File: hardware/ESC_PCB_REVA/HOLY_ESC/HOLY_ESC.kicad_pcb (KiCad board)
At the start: 4 copper layers, 69.1 x 39.2 mm, 77 parts, among them J1 Header, J2 Conn_01x06_Pin, J3 Header, Q1 BUK7Y1R4-40H, Q2 BUK7Y1R4-40H, Q3 BUK7Y1R4-40H, Q4 BUK7Y1R4-40H, Q5 BUK7Y1R4-40H, Q6 BUK7Y1R4-40H, U1 DRV8300DPWR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

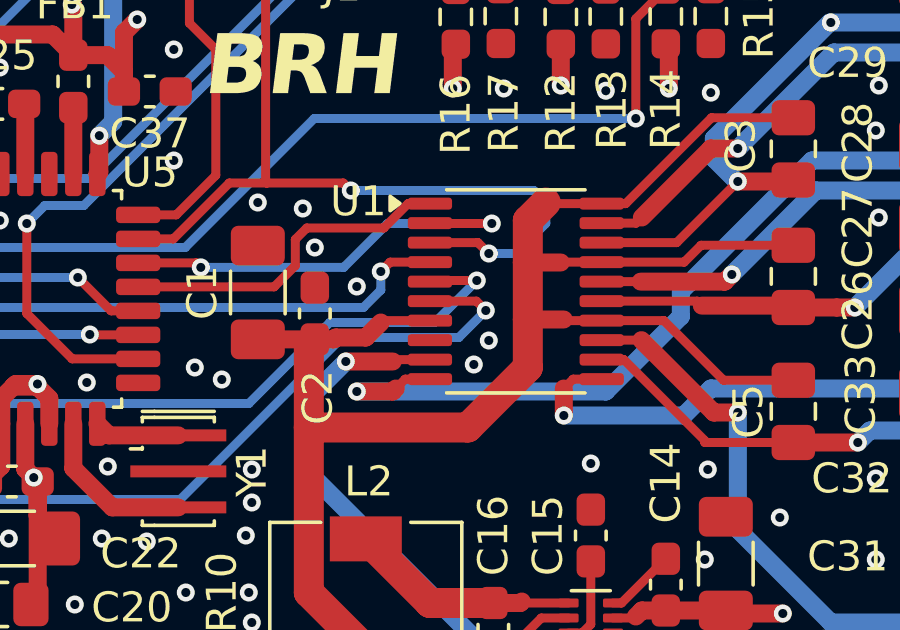
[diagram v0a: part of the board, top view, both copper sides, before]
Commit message: fix the REV A bst cap issue
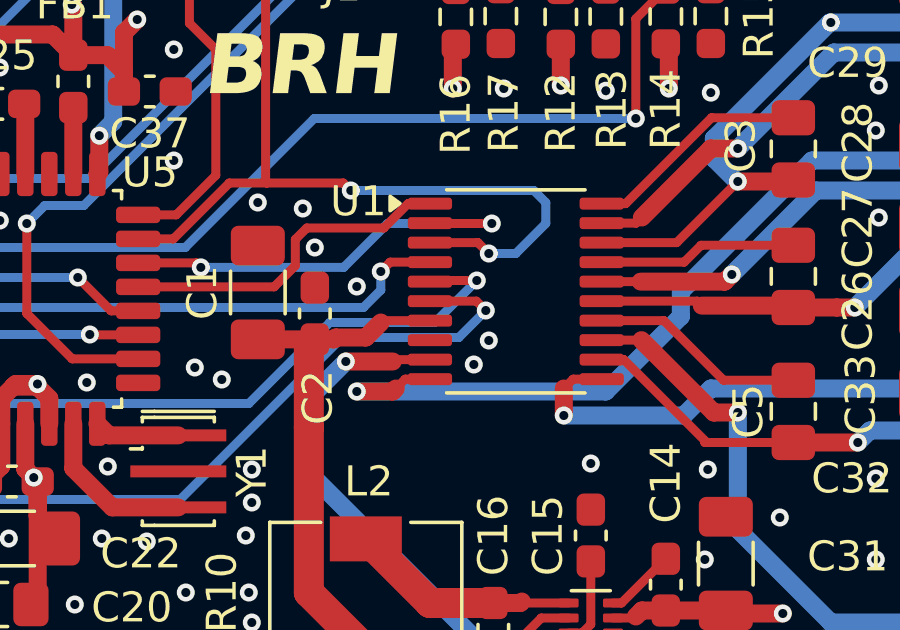
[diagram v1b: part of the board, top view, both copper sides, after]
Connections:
- C3 pad 1: +12V -> Net-(U1-BSTA)
- C4 pad 1: +12V -> Net-(U1-BSTB)
- C5 pad 1: +12V -> Net-(U1-BSTC)
- U1 pad 14: +12V -> Net-(U1-BSTC)
- U1 pad 17: +12V -> Net-(U1-BSTB)
- U1 pad 20: +12V -> Net-(U1-BSTA)
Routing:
- net +12V: track 90.7 -> 48.5 mm
- net Net-(U1-BSTA): track 0.00 -> 7.57 mm
- net Net-(U1-BSTC): track 0.00 -> 7.21 mm
- net Net-(U1-BSTB): track 0.00 -> 6.62 mm
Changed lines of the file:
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@@
 	(net 54 "Net-(D1-A)")
 	(net 55 "Net-(D2-A)")
+	(net 56 "Net-(U1-BSTA)")
+	(net 57 "Net-(U1-BSTB)")
+	(net 58 "Net-(U1-BSTC)")
 	(footprint "Package_TO_SOT_SMD:SOT-583-8"
 		(layer "F.Cu")
@@
 			(layers "F.Cu" "F.Mask" "F.Paste")
 			(roundrect_rratio 0.212766)
-			(net 1 "+12V")
+			(net 58 "Net-(U1-BSTC)")
 			(pintype "passive")
 		)
@@
 			(layers "F.Cu" "F.Mask" "F.Paste")
 			(roundrect_rratio 0.25)
-			(net 1 "+12V")
+			(net 58 "Net-(U1-BSTC)")
 			(pinfunction "BSTC")
 			(pintype "input")
@@
 			(layers "F.Cu" "F.Mask" "F.Paste")
 			(roundrect_rratio 0.25)
-			(net 1 "+12V")
+			(net 57 "Net-(U1-BSTB)")
 			(pinfunction "BSTB")
 			(pintype "input")
@@
 			(layers "F.Cu" "F.Mask" "F.Paste")
 			(roundrect_rratio 0.25)
-			(net 1 "+12V")
+			(net 56 "Net-(U1-BSTA)")
 			(pinfunction "BSTA")
 			(pintype "input")
@@
 			(layers "F.Cu" "F.Mask" "F.Paste")
 			(roundrect_rratio 0.212766)
-			(net 1 "+12V")
+			(net 56 "Net-(U1-BSTA)")
 			(pintype "passive")
 		)
@@
 			(layers "F.Cu" "F.Mask" "F.Paste")
 			(roundrect_rratio 0.212766)
-			(net 1 "+12V")
+			(net 57 "Net-(U1-BSTB)")
 			(pintype "passive")
 		)
@@
 	)
 	(segment
-		(start 173.675 82.325)
-		(end 176.75 82.325)
-		(width 0.3)
-		(layer "F.Cu")
-		(net 1)
-	)
-	(segment
 		(start 154.8625 99.9375)
 		(end 153.1875 101.6125)
@@
 	)
 	(segment
-		(start 167.9 86.4)
-		(end 167.9 84.8)
-		(width 1)
-		(layer "F.Cu")
-		(net 1)
-	)
-	(segment
-		(start 167.9 81.5)
-		(end 168.5 80.9)
-		(width 1)
-		(layer "F.Cu")
-		(net 1)
-	)
-	(segment
-		(start 169.0125 82.8875)
-		(end 169 82.9)
-		(width 0.3)
-		(layer "F.Cu")
-		(net 1)
-	)
-	(segment
-		(start 170.3625 80.9375)
-		(end 171.1625 80.9375)
-		(width 0.3)
-		(layer "F.Cu")
-		(net 1)
-	)
-	(segment
 		(start 153.1875 101.6125)
 		(end 150.825 101.6125)
@@
 	)
 	(segment
-		(start 167.9 84.8)
-		(end 167.9 82.9)
-		(width 1)
-		(layer "F.Cu")
-		(net 1)
-	)
-	(segment
 		(start 162.5 97.6125)
 		(end 162.5 99.2)
@@
 	)
 	(segment
-		(start 174.425 86.825)
-		(end 176.75 86.825)
-		(width 0.3)
-		(layer "F.Cu")
-		(net 1)
-	)
-	(segment
 		(start 164.2 99.25)
 		(end 162.55 99.25)
@@
 	)
 	(segment
-		(start 173.1125 82.8875)
-		(end 173.675 82.325)
-		(width 0.3)
-		(layer "F.Cu")
-		(net 1)
-	)
-	(segment
-		(start 167.9 82.9)
-		(end 167.9 81.5)
-		(width 1)
-		(layer "F.Cu")
-		(net 1)
-	)
-	(segment
 		(start 162.5 85.4)
 		(end 161.5 85.4)
@@
 	)
 	(segment
-		(start 170.3625 82.8875)
-		(end 173.1125 82.8875)
-		(width 0.3)
-		(layer "F.Cu")
-		(net 1)
-	)
-	(segment
 		(start 159.8 99.9375)
 		(end 157.3 99.9375)
@@
 	)
 	(segment
-		(start 169.1375 84.8375)
-		(end 169.1 84.8)
-		(width 0.3)
-		(layer "F.Cu")
-		(net 1)
-	)
-	(segment
 		(start 161.4375 85.4625)
 		(end 160.8 85.4625)
@@
 	)
 	(segment
-		(start 171.1625 80.9375)
-		(end 174.025 78.075)
-		(width 0.3)
-		(layer "F.Cu")
-		(net 1)
-	)
-	(segment
 		(start 162.5 97.6125)
 		(end 162.5 95.8)
@@
 	)
 	(segment
-		(start 170.3625 84.8375)
-		(end 172.4375 84.8375)
-		(width 0.3)
-		(layer "F.Cu")
-		(net 1)
-	)
-	(segment
-		(start 169 82.9)
-		(end 167.9 82.9)
-		(width 0.6)
-		(layer "F.Cu")
-		(net 1)
-	)
-	(segment
 		(start 165.3 99.25)
 		(end 164.2 99.25)
@@
 	)
 	(segment
-		(start 172.4375 84.8375)
-		(end 174.425 86.825)
-		(width 0.3)
-		(layer "F.Cu")
-		(net 1)
-	)
-	(segment
 		(start 163 84.9)
 		(end 162.5 85.4)
@@
 	)
 	(segment
-		(start 170.3625 82.8875)
-		(end 169.0125 82.8875)
-		(width 0.3)
-		(layer "F.Cu")
-		(net 1)
-	)
-	(segment
 		(start 162.55 99.25)
 		(end 162.5 99.2)
@@
 	)
 	(segment
-		(start 174.025 78.075)
-		(end 176.75 78.075)
-		(width 0.3)
-		(layer "F.Cu")
-		(net 1)
-	)
-	(segment
-		(start 170.3625 80.9375)
-		(end 168.5375 80.9375)
-		(width 0.3)
-		(layer "F.Cu")
-		(net 1)
-	)
-	(segment
-		(start 160.6 88.4)
-		(end 165.9 88.4)
-		(width 1)
-		(layer "F.Cu")
-		(net 1)
-	)
-	(segment
 		(start 162.5 95.8)
 		(end 160.6 93.9)
@@
 	)
 	(segment
-		(start 170.3625 84.8375)
-		(end 169.1375 84.8375)
-		(width 0.3)
-		(layer "F.Cu")
-		(net 1)
-	)
-	(segment
-		(start 168.5375 80.9375)
-		(end 168.5 80.9)
-		(width 0.3)
-		(layer "F.Cu")
-		(net 1)
-	)
-	(segment
 		(start 167.1375 99.25)
 		(end 165.3 99.25)
@@
 	)
 	(segment
-		(start 165.9 88.4)
-		(end 167.9 86.4)
-		(width 1)
-		(layer "F.Cu")
-		(net 1)
-	)
-	(segment
 		(start 150.825 101.6125)
 		(end 150.825 96.5125)
@@
 	)
 	(segment
-		(start 169.1 84.8)
-		(end 167.9 84.8)
-		(width 0.6)
-		(layer "F.Cu")
-		(net 1)
-	)
-	(segment
 		(start 162.5 99.2)
 		(end 161.7625 99.9375)
@@
 		(net 55)
 	)
+	(segment
+		(start 170.3625 80.9375)
+		(end 171.1625 80.9375)
+		(width 0.3)
+		(layer "F.Cu")
+		(net 56)
+	)
+	(segment
+		(start 171.1625 80.9375)
+		(end 174.025 78.075)
+		(width 0.3)
+		(layer "F.Cu")
+		(net 56)
+	)
+	(segment
+		(start 174.025 78.075)
+		(end 176.75 78.075)
+		(width 0.3)
+		(layer "F.Cu")
+		(net 56)
+	)
+	(segment
+		(start 173.675 82.325)
+		(end 176.75 82.325)
+		(width 0.3)
+		(layer "F.Cu")
+		(net 57)
+	)
+	(segment
+		(start 173.1125 82.8875)
+		(end 173.675 82.325)
+		(width 0.3)
+		(layer "F.Cu")
+		(net 57)
+	)
+	(segment
+		(start 170.3625 82.8875)
+		(end 173.1125 82.8875)
+		(width 0.3)
+		(layer "F.Cu")
+		(net 57)
+	)
+	(segment
+		(start 174.425 86.825)
+		(end 176.75 86.825)
+		(width 0.3)
+		(layer "F.Cu")
+		(net 58)
+	)
+	(segment
+		(start 170.3625 84.8375)
+		(end 172.4375 84.8375)
+		(width 0.3)
+		(layer "F.Cu")
+		(net 58)
+	)
+	(segment
+		(start 172.4375 84.8375)
+		(end 174.425 86.825)
+		(width 0.3)
+		(layer "F.Cu")
+		(net 58)
+	)
 	(zone
